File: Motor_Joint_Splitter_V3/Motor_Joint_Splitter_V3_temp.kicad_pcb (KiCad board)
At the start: 2 copper layers, 45 x 45 mm, 22 parts, among them J1 Conn_01x05, J2 26605030, J7 ethernet_54602-908LF, J8 motor_connector_292206-8, J9 Conn_01x05, U2 74ACT244MTCX

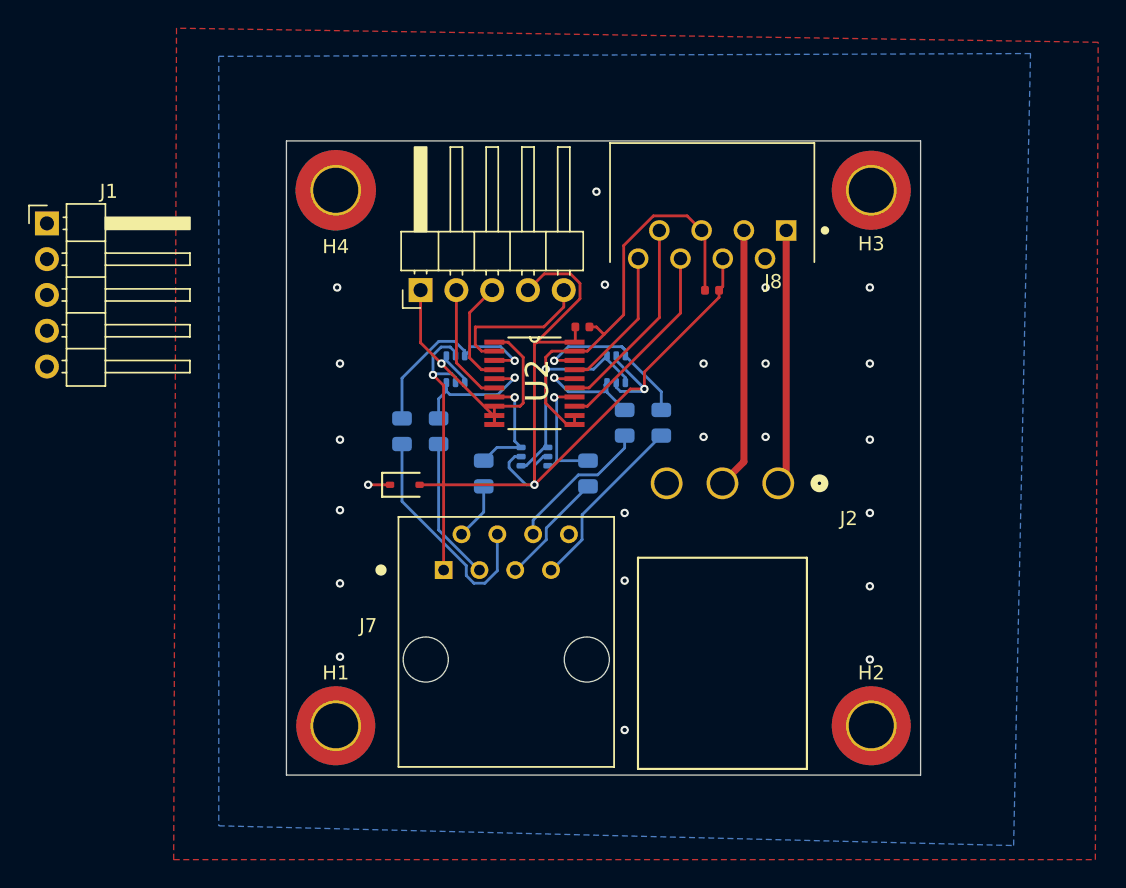
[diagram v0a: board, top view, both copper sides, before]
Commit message: Finished updating the joint splitter design. May want to consider using rows of single buffers rather than the octal buffer to prevent crosstalk.
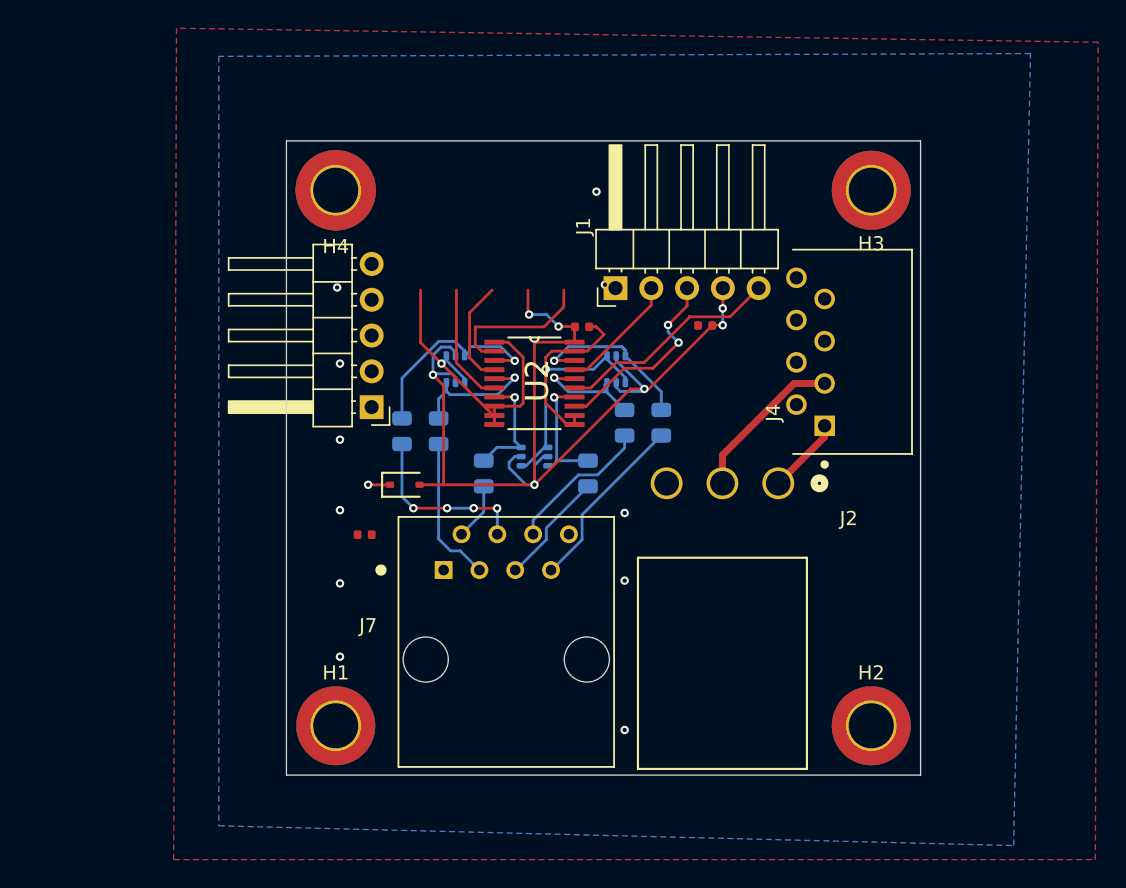
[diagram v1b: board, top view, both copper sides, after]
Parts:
- removed C2: 1uF, PCM_JLCPCB:C_0402
- removed J8: motor_connector_292206-8, splitter_parts:TE_292206-8
- added C3: 1uF, PCM_JLCPCB:C_0402, F.Cu at (201.0, 73.2)
- added C4: 1uF, PCM_JLCPCB:C_0402, F.Cu at (209.7, 73.1)
- added J4: motor_connector_292206-8, splitter_parts:TE_292206-8, F.Cu at (217.2, 75.0)
- moved J1 40.6 mm to (203.3, 70.4), turned to 90 degrees
- moved C1 30.1 mm to (185.6, 87.9)
- moved J9 9.00 mm to (186.1, 78.9), turned to 180 degrees
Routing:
- net GND: track 71.5 -> 53.4 mm, vias 25 -> 14
- net /Sin: track 18.2 -> 5.44 mm
- net +5V: track 86.3 -> 75.2 mm, vias 3 -> 7
- net /Cos: track 18.6 -> 11.4 mm
- net /C_I_Out_2: track 16.6 -> 12.7 mm, vias 0 -> 4
- net /C_B: track 14.3 -> 16.1 mm
- net /C_I: track 10.3 -> 8.55 mm
- net /C_A: track 14.1 -> 14.0 mm, vias 0 -> 2
